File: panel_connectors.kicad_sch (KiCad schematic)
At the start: 0 parts

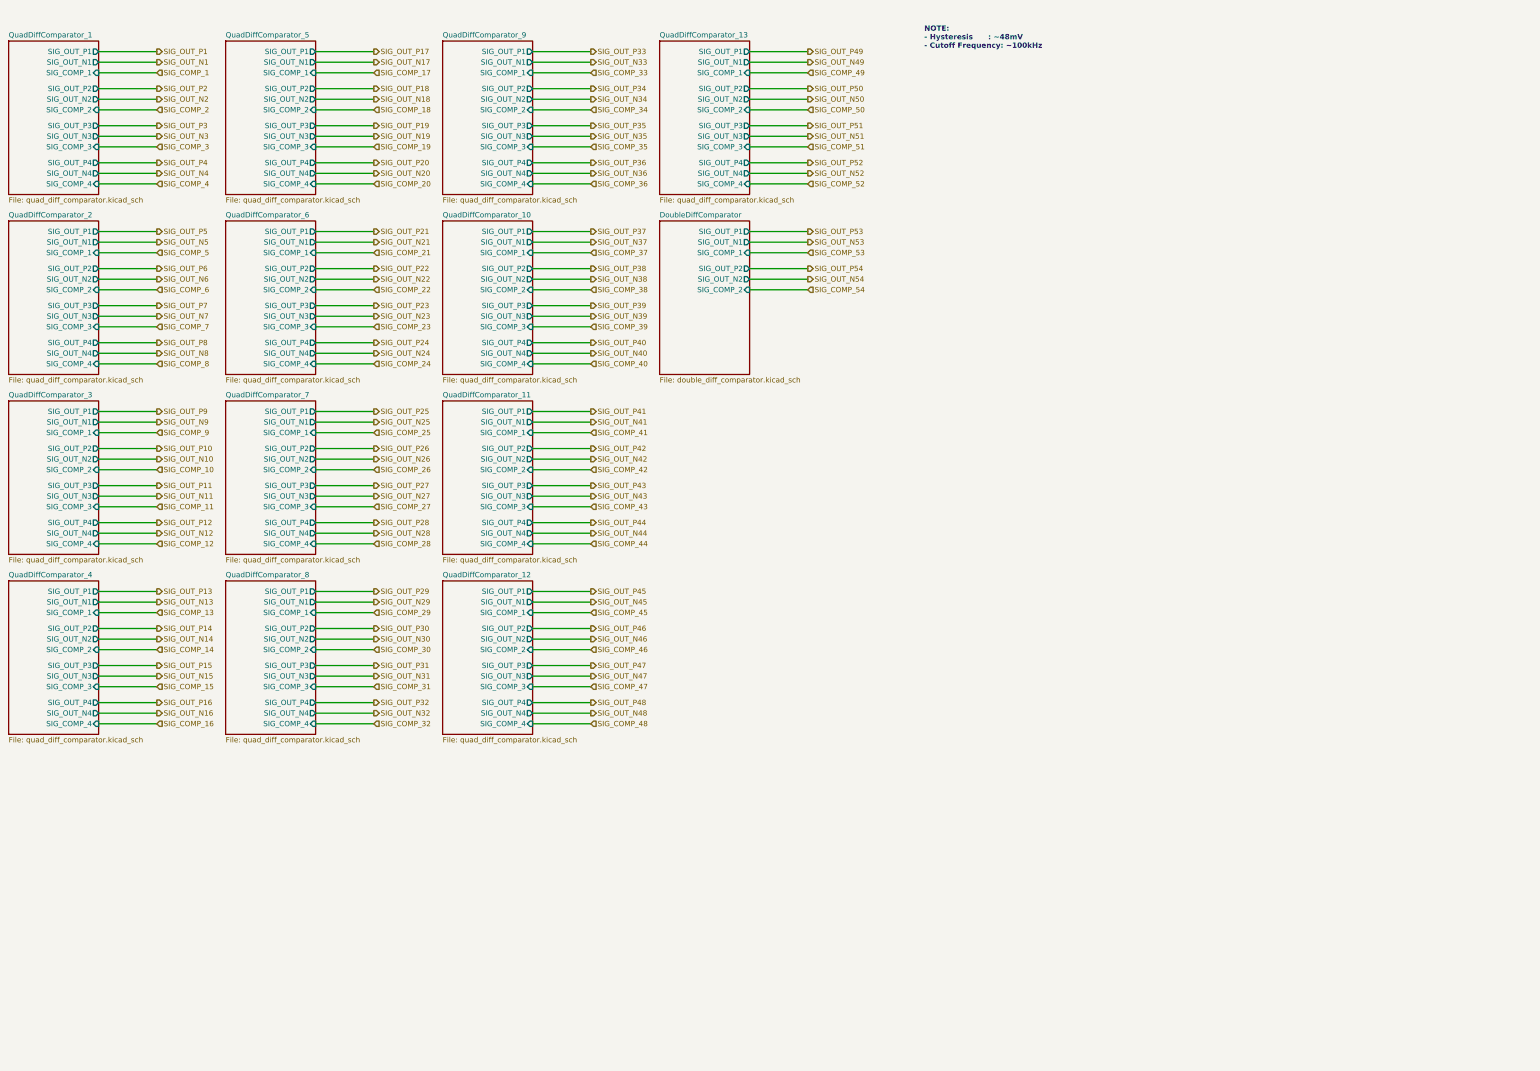
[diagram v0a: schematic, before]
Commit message: New design; reduce MCU pin count; utilize new connectors
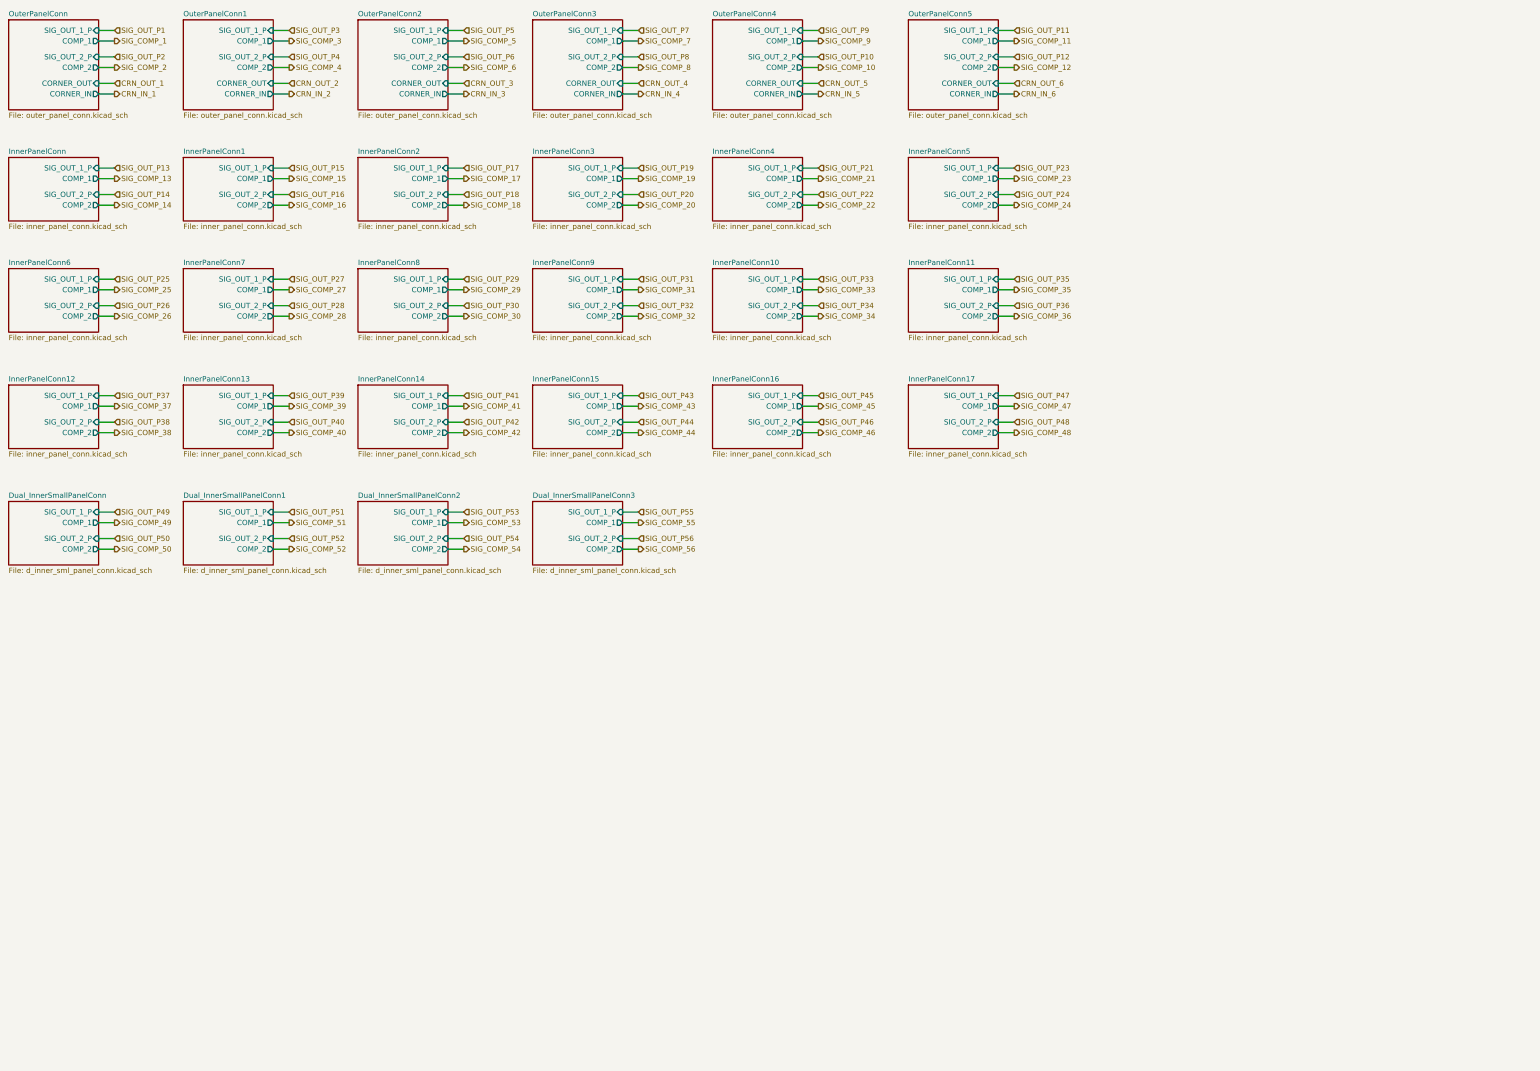
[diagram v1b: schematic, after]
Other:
- removed sheet DoubleDiffComparator
- removed sheet QuadDiffComparator_1
- removed sheet QuadDiffComparator_10
- removed sheet QuadDiffComparator_11
- removed sheet QuadDiffComparator_12
- removed sheet QuadDiffComparator_13
- removed sheet QuadDiffComparator_2
- removed sheet QuadDiffComparator_3
- removed sheet QuadDiffComparator_4
- removed sheet QuadDiffComparator_5
- removed sheet QuadDiffComparator_6
- removed sheet QuadDiffComparator_7
- removed sheet QuadDiffComparator_8
- removed sheet QuadDiffComparator_9
- added sheet Dual_InnerSmallPanelConn (d_inner_sml_panel_conn.kicad_sch)
- added sheet Dual_InnerSmallPanelConn1 (d_inner_sml_panel_conn.kicad_sch)
- added sheet Dual_InnerSmallPanelConn2 (d_inner_sml_panel_conn.kicad_sch)
- added sheet Dual_InnerSmallPanelConn3 (d_inner_sml_panel_conn.kicad_sch)
- added sheet InnerPanelConn (inner_panel_conn.kicad_sch)
- added sheet InnerPanelConn1 (inner_panel_conn.kicad_sch)
- added sheet InnerPanelConn10 (inner_panel_conn.kicad_sch)
- added sheet InnerPanelConn11 (inner_panel_conn.kicad_sch)
- added sheet InnerPanelConn12 (inner_panel_conn.kicad_sch)
- added sheet InnerPanelConn13 (inner_panel_conn.kicad_sch)
- added sheet InnerPanelConn14 (inner_panel_conn.kicad_sch)
- added sheet InnerPanelConn15 (inner_panel_conn.kicad_sch)
- added sheet InnerPanelConn16 (inner_panel_conn.kicad_sch)
- added sheet InnerPanelConn17 (inner_panel_conn.kicad_sch)
- added sheet InnerPanelConn2 (inner_panel_conn.kicad_sch)
- added sheet InnerPanelConn3 (inner_panel_conn.kicad_sch)
- added sheet InnerPanelConn4 (inner_panel_conn.kicad_sch)
- added sheet InnerPanelConn5 (inner_panel_conn.kicad_sch)
- added sheet InnerPanelConn6 (inner_panel_conn.kicad_sch)
- added sheet InnerPanelConn7 (inner_panel_conn.kicad_sch)
- added sheet InnerPanelConn8 (inner_panel_conn.kicad_sch)
- added sheet InnerPanelConn9 (inner_panel_conn.kicad_sch)
- added sheet OuterPanelConn (outer_panel_conn.kicad_sch)
- added sheet OuterPanelConn1 (outer_panel_conn.kicad_sch)
- added sheet OuterPanelConn2 (outer_panel_conn.kicad_sch)
- added sheet OuterPanelConn3 (outer_panel_conn.kicad_sch)
- added sheet OuterPanelConn4 (outer_panel_conn.kicad_sch)
- added sheet OuterPanelConn5 (outer_panel_conn.kicad_sch)
- note removed: "NOTE: - Hysteresis : ~48mV - Cutoff Frequency: ~100kHz"

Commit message: Cerberus complete.
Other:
- removed sheet InnerPanelConn16
- removed sheet InnerPanelConn17
- sheet Dual_InnerSmallPanelConn ports: added BUS_EN_1, BUS_EN_2, DIFF_IN_+, DIFF_IN_-, DIFF_OUT_+, DIFF_OUT_-; removed COMP_1, COMP_2, SIG_OUT_1_P, SIG_OUT_2_P
- sheet Dual_InnerSmallPanelConn1 ports: added BUS_EN_1, BUS_EN_2, DIFF_IN_+, DIFF_IN_-, DIFF_OUT_+, DIFF_OUT_-; removed COMP_1, COMP_2, SIG_OUT_1_P, SIG_OUT_2_P
- sheet Dual_InnerSmallPanelConn2 ports: added BUS_EN_1, BUS_EN_2, DIFF_IN_+, DIFF_IN_-, DIFF_OUT_+, DIFF_OUT_-; removed COMP_1, COMP_2, SIG_OUT_1_P, SIG_OUT_2_P
- sheet Dual_InnerSmallPanelConn3 ports: added BUS_EN_1, BUS_EN_2, DIFF_IN_+, DIFF_IN_-, DIFF_OUT_+, DIFF_OUT_-; removed COMP_1, COMP_2, SIG_OUT_1_P, SIG_OUT_2_P
- sheet InnerPanelConn ports: added BUS_EN_1, BUS_EN_2, DIFF_IN_+, DIFF_IN_-, DIFF_OUT_+, DIFF_OUT_-; removed COMP_1, COMP_2, SIG_OUT_1_P, SIG_OUT_2_P
- sheet InnerPanelConn1 ports: added BUS_EN_1, BUS_EN_2, DIFF_IN_+, DIFF_IN_-, DIFF_OUT_+, DIFF_OUT_-; removed COMP_1, COMP_2, SIG_OUT_1_P, SIG_OUT_2_P
- sheet InnerPanelConn10 ports: added BUS_EN_1, BUS_EN_2, DIFF_IN_+, DIFF_IN_-, DIFF_OUT_+, DIFF_OUT_-; removed COMP_1, COMP_2, SIG_OUT_1_P, SIG_OUT_2_P
- sheet InnerPanelConn11 ports: added BUS_EN_1, BUS_EN_2, DIFF_IN_+, DIFF_IN_-, DIFF_OUT_+, DIFF_OUT_-; removed COMP_1, COMP_2, SIG_OUT_1_P, SIG_OUT_2_P
- sheet InnerPanelConn12 ports: added BUS_EN_1, BUS_EN_2, DIFF_IN_+, DIFF_IN_-, DIFF_OUT_+, DIFF_OUT_-; removed COMP_1, COMP_2, SIG_OUT_1_P, SIG_OUT_2_P
- sheet InnerPanelConn13 ports: added BUS_EN_1, BUS_EN_2, DIFF_IN_+, DIFF_IN_-, DIFF_OUT_+, DIFF_OUT_-; removed COMP_1, COMP_2, SIG_OUT_1_P, SIG_OUT_2_P
- sheet InnerPanelConn14 ports: added BUS_EN_1, BUS_EN_2, DIFF_IN_+, DIFF_IN_-, DIFF_OUT_+, DIFF_OUT_-; removed COMP_1, COMP_2, SIG_OUT_1_P, SIG_OUT_2_P
- sheet InnerPanelConn15 ports: added BUS_EN_1, BUS_EN_2, DIFF_IN_+, DIFF_IN_-, DIFF_OUT_+, DIFF_OUT_-; removed COMP_1, COMP_2, SIG_OUT_1_P, SIG_OUT_2_P
- sheet InnerPanelConn2 ports: added BUS_EN_1, BUS_EN_2, DIFF_IN_+, DIFF_IN_-, DIFF_OUT_+, DIFF_OUT_-; removed COMP_1, COMP_2, SIG_OUT_1_P, SIG_OUT_2_P
- sheet InnerPanelConn3 ports: added BUS_EN_1, BUS_EN_2, DIFF_IN_+, DIFF_IN_-, DIFF_OUT_+, DIFF_OUT_-; removed COMP_1, COMP_2, SIG_OUT_1_P, SIG_OUT_2_P
- sheet InnerPanelConn4 ports: added BUS_EN_1, BUS_EN_2, DIFF_IN_+, DIFF_IN_-, DIFF_OUT_+, DIFF_OUT_-; removed COMP_1, COMP_2, SIG_OUT_1_P, SIG_OUT_2_P
- sheet InnerPanelConn5 ports: added BUS_EN_1, BUS_EN_2, DIFF_IN_+, DIFF_IN_-, DIFF_OUT_+, DIFF_OUT_-; removed COMP_1, COMP_2, SIG_OUT_1_P, SIG_OUT_2_P
- sheet InnerPanelConn6 ports: added BUS_EN_1, BUS_EN_2, DIFF_IN_+, DIFF_IN_-, DIFF_OUT_+, DIFF_OUT_-; removed COMP_1, COMP_2, SIG_OUT_1_P, SIG_OUT_2_P
- sheet InnerPanelConn7 ports: added BUS_EN_1, BUS_EN_2, DIFF_IN_+, DIFF_IN_-, DIFF_OUT_+, DIFF_OUT_-; removed COMP_1, COMP_2, SIG_OUT_1_P, SIG_OUT_2_P
- sheet InnerPanelConn8 ports: added BUS_EN_1, BUS_EN_2, DIFF_IN_+, DIFF_IN_-, DIFF_OUT_+, DIFF_OUT_-; removed COMP_1, COMP_2, SIG_OUT_1_P, SIG_OUT_2_P
- sheet InnerPanelConn9 ports: added BUS_EN_1, BUS_EN_2, DIFF_IN_+, DIFF_IN_-, DIFF_OUT_+, DIFF_OUT_-; removed COMP_1, COMP_2, SIG_OUT_1_P, SIG_OUT_2_P
- sheet OuterPanelConn ports: added BUS_EN_1, BUS_EN_2, DIFF_IN_+, DIFF_IN_-, DIFF_OUT_+, DIFF_OUT_-; removed COMP_1, COMP_2, SIG_OUT_1_P, SIG_OUT_2_P
- sheet OuterPanelConn1 ports: added BUS_EN_1, BUS_EN_2, DIFF_IN_+, DIFF_IN_-, DIFF_OUT_+, DIFF_OUT_-; removed COMP_1, COMP_2, SIG_OUT_1_P, SIG_OUT_2_P
- sheet OuterPanelConn2 ports: added BUS_EN_1, BUS_EN_2, DIFF_IN_+, DIFF_IN_-, DIFF_OUT_+, DIFF_OUT_-; removed COMP_1, COMP_2, SIG_OUT_1_P, SIG_OUT_2_P
- sheet OuterPanelConn3 ports: added BUS_EN_1, BUS_EN_2, DIFF_IN_+, DIFF_IN_-, DIFF_OUT_+, DIFF_OUT_-; removed COMP_1, COMP_2, SIG_OUT_1_P, SIG_OUT_2_P
- sheet OuterPanelConn4 ports: added BUS_EN_1, BUS_EN_2, DIFF_IN_+, DIFF_IN_-, DIFF_OUT_+, DIFF_OUT_-; removed COMP_1, COMP_2, SIG_OUT_1_P, SIG_OUT_2_P
- sheet OuterPanelConn5 ports: added BUS_EN_1, BUS_EN_2, DIFF_IN_+, DIFF_IN_-, DIFF_OUT_+, DIFF_OUT_-; removed COMP_1, COMP_2, SIG_OUT_1_P, SIG_OUT_2_P
